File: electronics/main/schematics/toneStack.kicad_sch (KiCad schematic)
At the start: 22 parts, among them U11 500pF 500V 5%, U12 500pF 500V 5%, U13 500pF 500V 5%, U14 22n 630V 5%, U15 22n 630V 5%, U16 500pF 500V 5%

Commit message: schematic ready? - check
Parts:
- Audio-To-FX1: renamed from Audio-To-FX; footprint (none) -> TestPoint:TestPoint_THTPad_D2.0mm_Drill1.0mm
- Audo-From-FX1: renamed from Audo-From-FX; footprint (none) -> TestPoint:TestPoint_THTPad_D2.0mm_Drill1.0mm
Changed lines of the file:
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@@
 		(dnp no)
 		(fields_autoplaced yes)
-		(property "Reference" "Audio-To-FX"
+		(property "Reference" "Audio-To-FX1"
 			(at 279.4 143.5099 0)
 			(effects
@@
 			)
 		)
-		(property "Footprint" ""
+		(property "Footprint" "TestPoint:TestPoint_THTPad_D2.0mm_Drill1.0mm"
 			(at 283.21 144.78 0)
 			(effects
@@
 			(project "wb50"
 				(path "/6805e3ef-87bd-473d-890f-05ae2da73c1a/f74de693-82a9-4691-89de-552f27ba6ee3"
-					(reference "Audio-To-FX")
+					(reference "Audio-To-FX1")
 					(unit 1)
 				)
@@
 		(dnp no)
 		(fields_autoplaced yes)
-		(property "Reference" "Audo-From-FX"
+		(property "Reference" "Audo-From-FX1"
 			(at 297.18 143.5099 0)
 			(effects
@@
 			)
 		)
-		(property "Footprint" ""
+		(property "Footprint" "TestPoint:TestPoint_THTPad_D2.0mm_Drill1.0mm"
 			(at 300.99 144.78 0)
 			(effects
@@
 			(project "wb50"
 				(path "/6805e3ef-87bd-473d-890f-05ae2da73c1a/f74de693-82a9-4691-89de-552f27ba6ee3"
-					(reference "Audo-From-FX")
-					(unit 1)
-				)
+					(reference "Audo-From-FX1")
+					(unit 1)
+				)

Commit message: schematic  checked!
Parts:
- added D6: UF4007_C960666, footprints:DO-41_BD2.4-L4.7-P8.70-D0.9-RD, symbol jlcpcb:UF4007_C960666
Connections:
- net +12V: now also RELAY3.2, D6.1 (K)
- net GND-AUD: now also RV5.1, RV6.1; no longer RV5.3, RV6.3
- net REL-SW: now reaches RELAY3.9
- net REL-SW: now also D6.2 (A)
- new net: Audo-From-FX1.1, RV5.3, RV6.3
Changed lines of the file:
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@@
 	)
 	(junction
+		(at 349.25 144.78)
+		(diameter 0)
+		(color 0 0 0 0)
+	)
+	(junction
 		(at 134.62 144.78)
 		(diameter 0)
@@
 	(wire
 		(pts
+			(xy 349.25 133.35) (xy 349.25 144.78)
+		)
+		(stroke
+			(width 0)
+			(type default)
+		)
+	)
+	(wire
+		(pts
+			(xy 349.25 144.78) (xy 360.68 144.78)
+		)
+		(stroke
+			(width 0)
+			(type default)
+		)
+	)
+	(wire
+		(pts
 			(xy 195.58 160.02) (xy 195.58 162.56)
 		)
@@
 	(wire
 		(pts
+			(xy 349.25 177.8) (xy 349.25 184.15)
+		)
+		(stroke
+			(width 0)
+			(type default)
+		)
+	)
+	(wire
+		(pts
 			(xy 309.88 144.78) (xy 309.88 176.53)
 		)
@@
 	(wire
 		(pts
+			(xy 349.25 144.78) (xy 349.25 157.48)
+		)
+		(stroke
+			(width 0)
+			(type default)
+		)
+	)
+	(wire
+		(pts
 			(xy 172.72 63.5) (xy 172.72 60.96)
 		)
@@
 		)
 	)
+	(global_label "REL-SW"
+		(shape input)
+		(at 349.25 184.15 270)
+		(fields_autoplaced yes)
+		(effects
+			(font
+				(size 1.27 1.27)
+			)
+			(justify right)
+		)
+		(property "Intersheetrefs" "${INTERSHEET_REFS}"
+			(at 349.25 194.8156 90)
+			(effects
+				(font
+					(size 1.27 1.27)
+				)
+				(justify right)
+				(hide yes)
+			)
+		)
+	)
+	(global_label "REL-SW"
+		(shape input)
+		(at 370.84 144.78 0)
+		(fields_autoplaced yes)
+		(effects
+			(font
+				(size 1.27 1.27)
+			)
+			(justify left)
+		)
+		(property "Intersheetrefs" "${INTERSHEET_REFS}"
+			(at 381.5056 144.78 0)
+			(effects
+				(font
+					(size 1.27 1.27)
+				)
+				(justify left)
+				(hide yes)
+			)
+		)
+	)
 	(global_label "HV-D"
 		(shape passive)
@@
 	)
 	(symbol
+		(lib_id "power:+12V")
+		(at 349.25 133.35 0)
+		(unit 1)
+		(exclude_from_sim no)
+		(in_bom yes)
+		(on_board yes)
+		(dnp no)
+		(fields_autoplaced yes)
+		(property "Reference" "#PWR042"
+			(at 349.25 137.16 0)
+			(effects
+				(font
+					(size 1.27 1.27)
+				)
+				(hide yes)
+			)
+		)
+		(property "Value" "+12V"
+			(at 349.25 128.27 0)
+			(effects
+				(font
+					(size 1.27 1.27)
+				)
+			)
+		)
+		(property "Footprint" ""
+			(at 349.25 133.35 0)
+			(effects
+				(font
+					(size 1.27 1.27)
+				)
+				(hide yes)
+			)
+		)
+		(property "Datasheet" ""
+			(at 349.25 133.35 0)
+			(effects
+				(font
+					(size 1.27 1.27)
+				)
+				(hide yes)
+			)
+		)
+		(property "Description" "Power symbol creates a global label with name \"+12V\""
+			(at 349.25 133.35 0)
+			(effects
+				(font
+					(size 1.27 1.27)
+				)
+				(hide yes)
+			)
+		)
+		(pin "1"
+		)
+		(instances
+			(project "wb50"
+				(path "/6805e3ef-87bd-473d-890f-05ae2da73c1a/f74de693-82a9-4691-89de-552f27ba6ee3"
+					(reference "#PWR042")
+					(unit 1)
+				)
+			)
+		)
+	)
+	(symbol
 		(lib_id "power:GND")
 		(at 262.89 182.88 0)
@@
 		(lib_id "Device:R_Potentiometer")
 		(at 318.77 156.21 0)
+		(mirror x)
 		(unit 1)
 		(exclude_from_sim no)
@@
 		(on_board yes)
 		(dnp no)
-		(fields_autoplaced yes)
 		(property "Reference" "RV6"
 			(at 316.23 154.9399 0)
@@
 	)
 	(symbol
+		(lib_id "jlcpcb:UF4007_C960666")
+		(at 365.76 144.78 0)
+		(unit 1)
+		(exclude_from_sim no)
+		(in_bom yes)
+		(on_board yes)
+		(dnp no)
+		(fields_autoplaced yes)
+		(property "Reference" "D6"
+			(at 365.76 151.13 0)
+			(effects
+				(font
+					(size 1.27 1.27)
+				)
+			)
+		)
+		(property "Value" "UF4007_C960666"
+			(at 365.76 148.59 0)
+			(effects
+				(font
+					(size 1.27 1.27)
+				)
+			)
+		)
+		(property "Footprint" "footprints:DO-41_BD2.4-L4.7-P8.70-D0.9-RD"
+			(at 365.76 154.94 0)
+			(effects
+				(font
+					(size 1.27 1.27)
+					(italic yes)
+				)
+				(hide yes)
+			)
+		)
+		(property "Datasheet" "https://item.szlcsc.com/85412.html"
+			(at 363.474 144.653 0)
+			(effects
+				(font
+					(size 1.27 1.27)
+				)
+				(justify left)
+				(hide yes)
+			)
+		)
+		(property "Description" ""
+			(at 365.76 144.78 0)
+			(effects
+				(font
+					(size 1.27 1.27)
+				)
+				(hide yes)
+			)
+		)
+		(property "LCSC" "C960666"
+			(at 365.76 144.78 0)
+			(effects
+				(font
+					(size 1.27 1.27)
+				)
+				(hide yes)
+			)
+		)
+		(pin "1"
+		)
+		(pin "2"
+		)
+		(instances
+			(project "wb50"
+				(path "/6805e3ef-87bd-473d-890f-05ae2da73c1a/f74de693-82a9-4691-89de-552f27ba6ee3"
+					(reference "D6")
+					(unit 1)
+				)
+			)
+		)
+	)
+	(symbol
 		(lib_id "jlcpcb:RD50T5821J")
 		(at 134.62 152.4 270)
@@
 	)
 	(symbol
-		(lib_name "G5V-1-12V_1")
 		(lib_id "jlcpcb:G5V-1-12V")
 		(at 350.52 167.64 0)
@@
 		(lib_id "Device:R_Potentiometer")
 		(at 309.88 180.34 0)
+		(mirror x)
 		(unit 1)
 		(exclude_from_sim no)
@@
 		(on_board yes)
 		(dnp no)
-		(fields_autoplaced yes)
 		(property "Reference" "RV5"
 			(at 307.34 179.0699 0)

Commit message: updated PCB
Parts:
- Audio-To-FX1, Audo-From-FX1: footprint TestPoint:TestPoint_THTPad_D2.0mm_Drill1.0mm -> TestPoint:TestPoint_THTPad_D3.0mm_Drill1.5mm
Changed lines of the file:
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@@
 			)
 		)
-		(property "Footprint" "TestPoint:TestPoint_THTPad_D2.0mm_Drill1.0mm"
+		(property "Footprint" "TestPoint:TestPoint_THTPad_D3.0mm_Drill1.5mm"
 			(at 283.21 144.78 0)
 			(effects
@@
 			)
 		)
-		(property "Footprint" "TestPoint:TestPoint_THTPad_D2.0mm_Drill1.0mm"
+		(property "Footprint" "TestPoint:TestPoint_THTPad_D3.0mm_Drill1.5mm"
 			(at 300.99 144.78 0)
 			(effects

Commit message: update design
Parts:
- renumbered Audo-From-FX1 to Audio-From-FX1
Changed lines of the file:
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@@
 		(dnp no)
 		(fields_autoplaced yes)
-		(property "Reference" "Audo-From-FX1"
+		(property "Reference" "Audio-From-FX1"
 			(at 297.18 143.5099 0)
 			(effects
@@
 			(project "wb50"
 				(path "/6805e3ef-87bd-473d-890f-05ae2da73c1a/f74de693-82a9-4691-89de-552f27ba6ee3"
-					(reference "Audo-From-FX1")
+					(reference "Audio-From-FX1")
 					(unit 1)
 				)

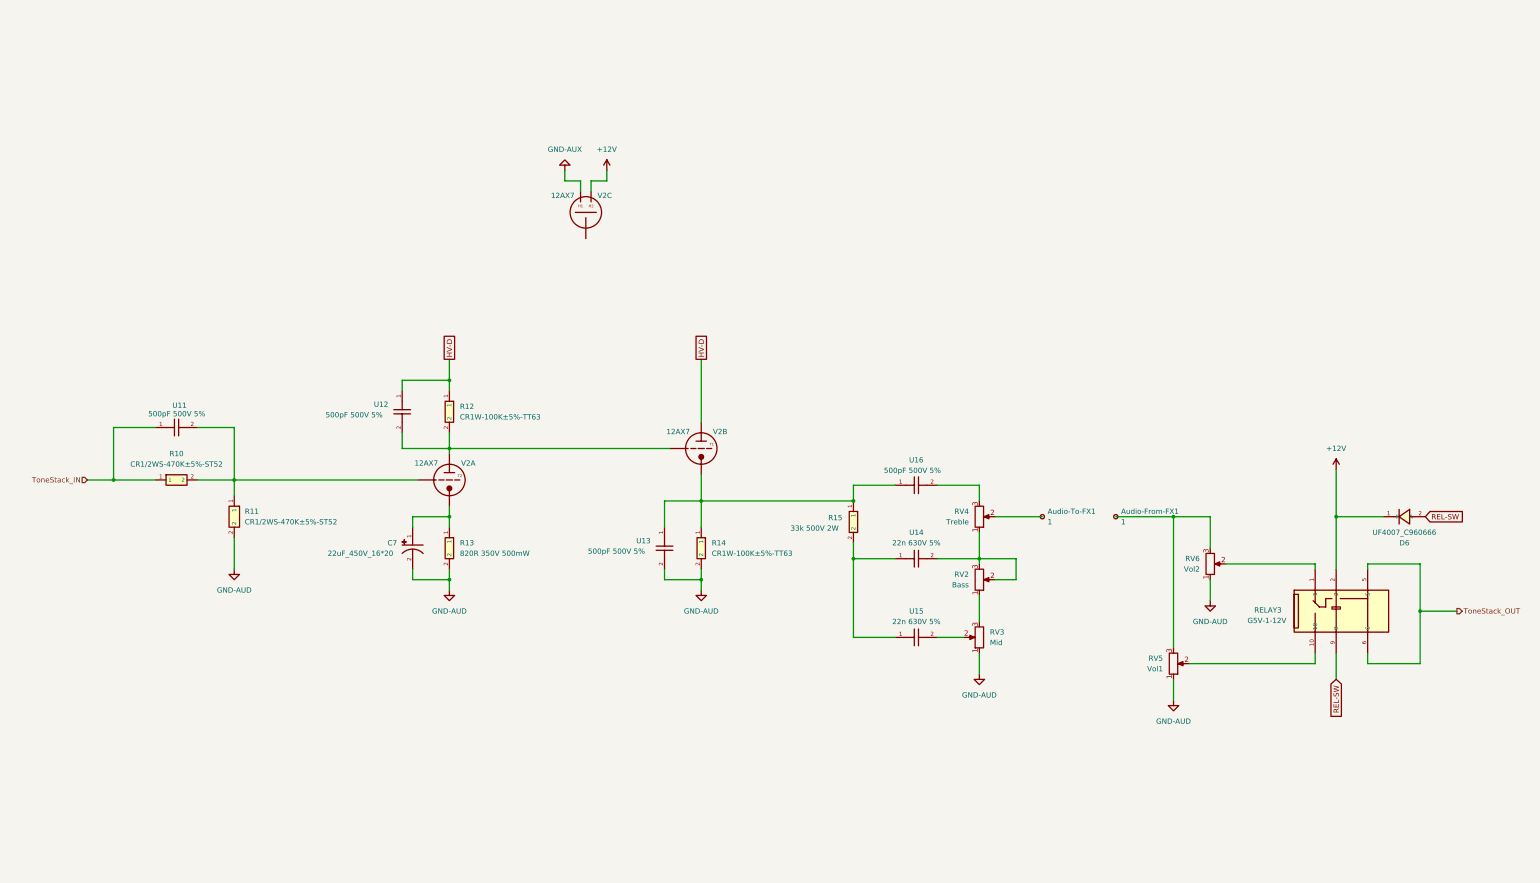
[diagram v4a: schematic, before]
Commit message: add fx loop, add new shield
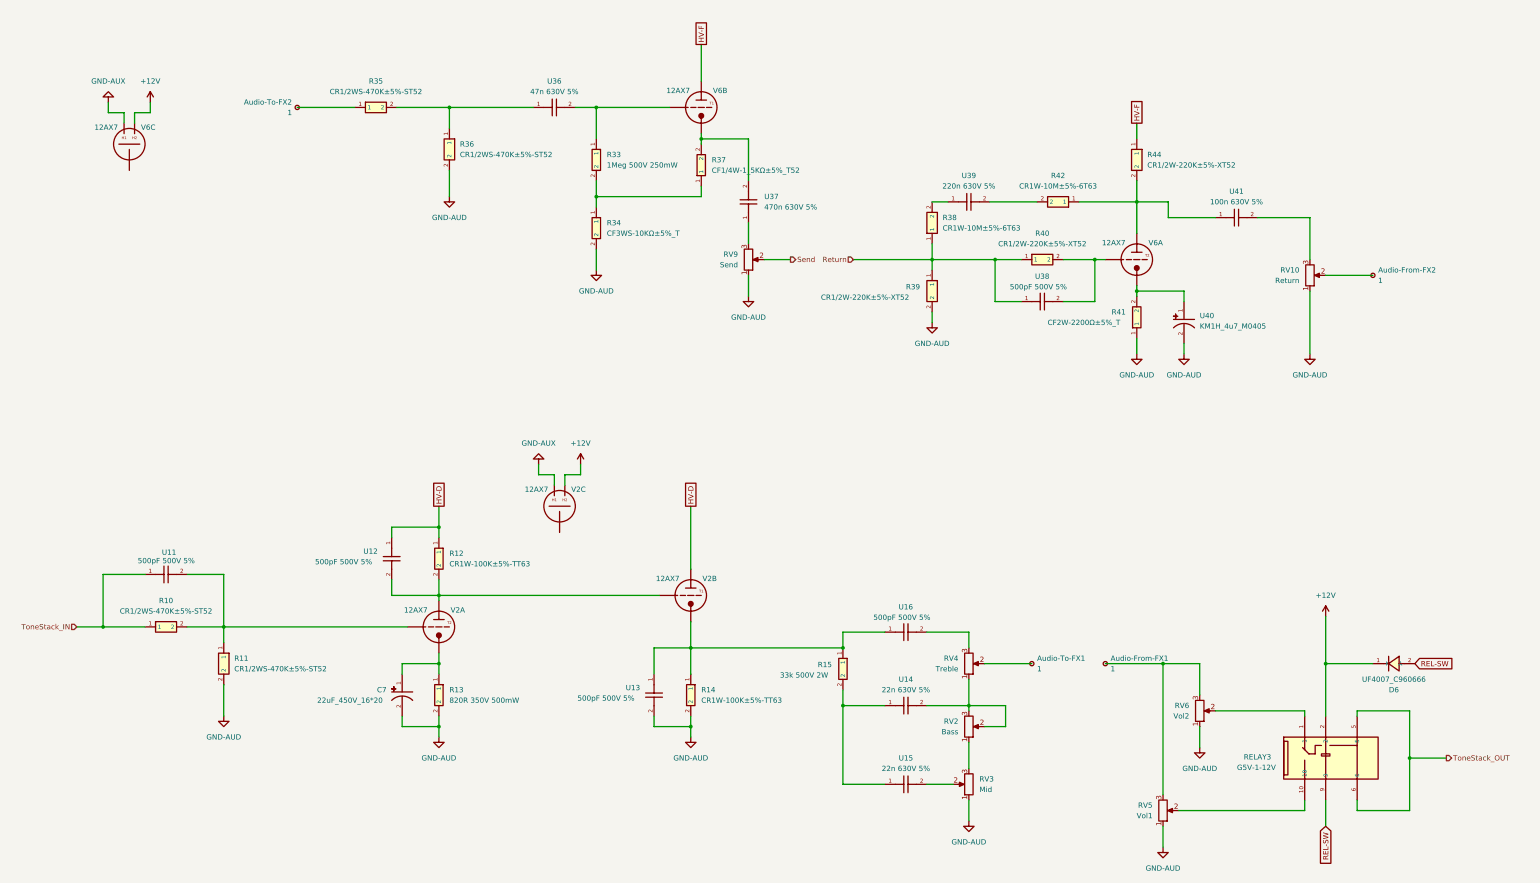
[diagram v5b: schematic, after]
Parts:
- added Audio-From-FX2, Audio-To-FX2: 1, TestPoint:TestPoint_THTPad_D3.0mm_Drill1.5mm, symbol Connector:TestPoint_Small
- added R33: 1Meg 500V 250mW, footprints:RES-TH_BD2.4-L6.3-P10.30-D0.6, symbol jlcpcb:CFR-25JT-52-1M
- added R34: CF3WS-10KΩ±5%_T, footprints:RES-TH_BD5.5-L15.0-P19.00-D0.8, symbol symbols:CF3WS-10KΩ±5%_T
- added R35, R36: CR1/2WS-470K±5%-ST52, footprints:RES-TH_BD2.7-L6.2-P10.20-D0.4, symbol symbols:CR1/2WS-470K±5%-ST52
- added R37: CF1/4W-1_5KΩ±5%_T52, footprints:RES-TH_BD2.3-L6.5-P10.50-D0.5, symbol symbols:CF1/4W-1_5KΩ±5%_T52
- added R38, R42: CR1W-10M±5%-6T63, footprints:RES-TH_BD4.5-L11.0-P15.00-D0.7, symbol symbols:CR1W-10M±5%-6T63
- added R39, R40, R44: CR1/2W-220K±5%-XT52, footprints:RES-TH_BD3.5-L9.0-P13.00-D0.5, symbol symbols:CR1/2W-220K±5%-XT52
- added R41: CF2W-2200Ω±5%_T, footprints:RES-TH_BD5.5-L15.0-P19.00-D0.8, symbol symbols:CF2W-2200Ω±5%_T
- added RV10: Return, wb50_footprints:WB50_Pot_Omeg_PC20BU_P5.00mm, symbol Device:R_Potentiometer
- added RV9: Send, wb50_footprints:WB50_Pot_Omeg_PC20BU_P5.00mm, symbol Device:R_Potentiometer
- added U36: 47n 630V 5%, wb50_footprints:MUSTARD_CAP_D8.5_L20.5_P25.5, symbol wb50_symbols:YellowCap_4n7_630V
- added U37: 470n 630V 5%, wb50_footprints:MUSTARD_CAP_D10_L32_P40.4, symbol wb50_symbols:YellowCap_100n_630V
- added U38: 500pF 500V 5%, wb50_footprints:MICA_CAP_L15.5_W3.6_P8.7, symbol wb50_symbols:MicaCap_500pf_500V
- added U39: 220n 630V 5%, wb50_footprints:MUSTARD_CAP_D10_L32_P40.4, symbol wb50_symbols:YellowCap_100n_630V
- added U40: KM1H_4u7_M0405, footprints:CAP-TH_BD4.0-P1.50-D0.5-FD, symbol symbols:KM1H4R7M0405
- added U41: 100n 630V 5%, wb50_footprints:MUSTARD_CAP_D10_L32_P40.4, symbol wb50_symbols:YellowCap_100n_630V
- added V6: 12AX7, wb50_footprints:WB50_Socket_Noval_9Pin_D21.0mm_Hole1.8mm, symbol wb50_symbols:WB50_12AX7
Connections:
- net +12V: now also V6.4 (H1)
- net GND-AUD: now also R34.2, R36.2, R39.2, R41.1, RV10.1, RV9.1, U40.2
- net GND-AUX: now also V6.5 (H2)
- new net: Audio-To-FX2.1, R35.1
- new net: R35.2, R36.1, U36.1
- new net: R42.1, R44.2, U41.1, V6.1 (A/P)
- new net: R40.2, U38.2, V6.2 (G)
- new net: R41.2, U40.1, V6.3 (C/K)
- new net: R42.2, U39.2
- new net: Audio-From-FX2.1, RV10.2
- new net: R33.2, R34.1, R37.1
- new net: R37.2, U37.2, V6.8 (C/K)
- new net: R38.2, U39.1
- new net: R33.1, U36.2, V6.7 (G)
- new net: RV9.3, U37.1
- new net: RV10.3, U41.2
- new net HV-F: R44.1, V6.6 (A/P)
- new net Return: R38.1, R39.1, R40.1, U38.1
- new net Send: RV9.2
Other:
- moved on the sheet: Audio-From-FX1, Audio-To-FX1, C7, D6, R10, R11, R12, R13, R14, R15, RELAY3, RV2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
